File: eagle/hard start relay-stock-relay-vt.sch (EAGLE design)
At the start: 0 parts

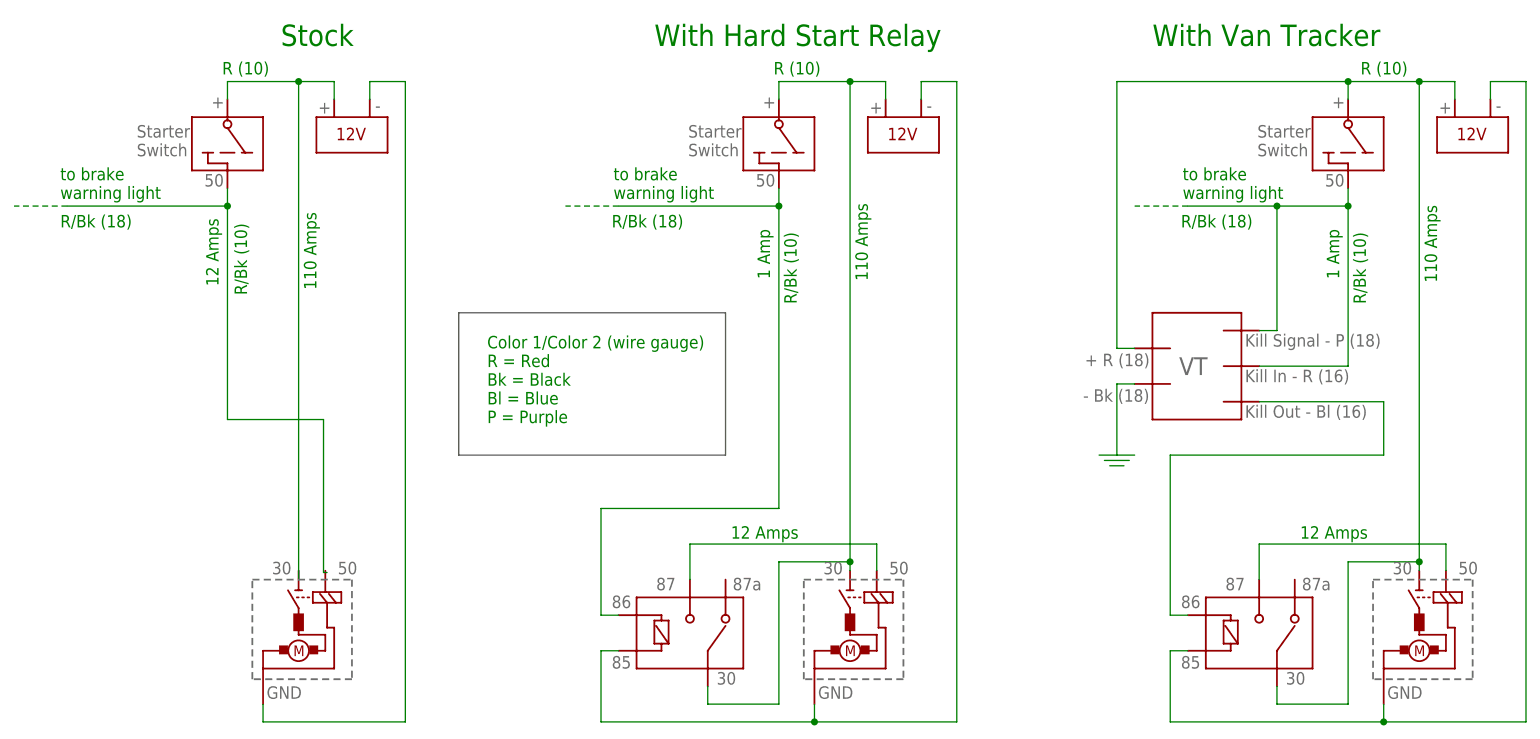
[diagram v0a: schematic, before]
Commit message: 1.kill signal is now also the line that's being interrupted 2.remove starter wire that goes to emergency brake warning light, etc.
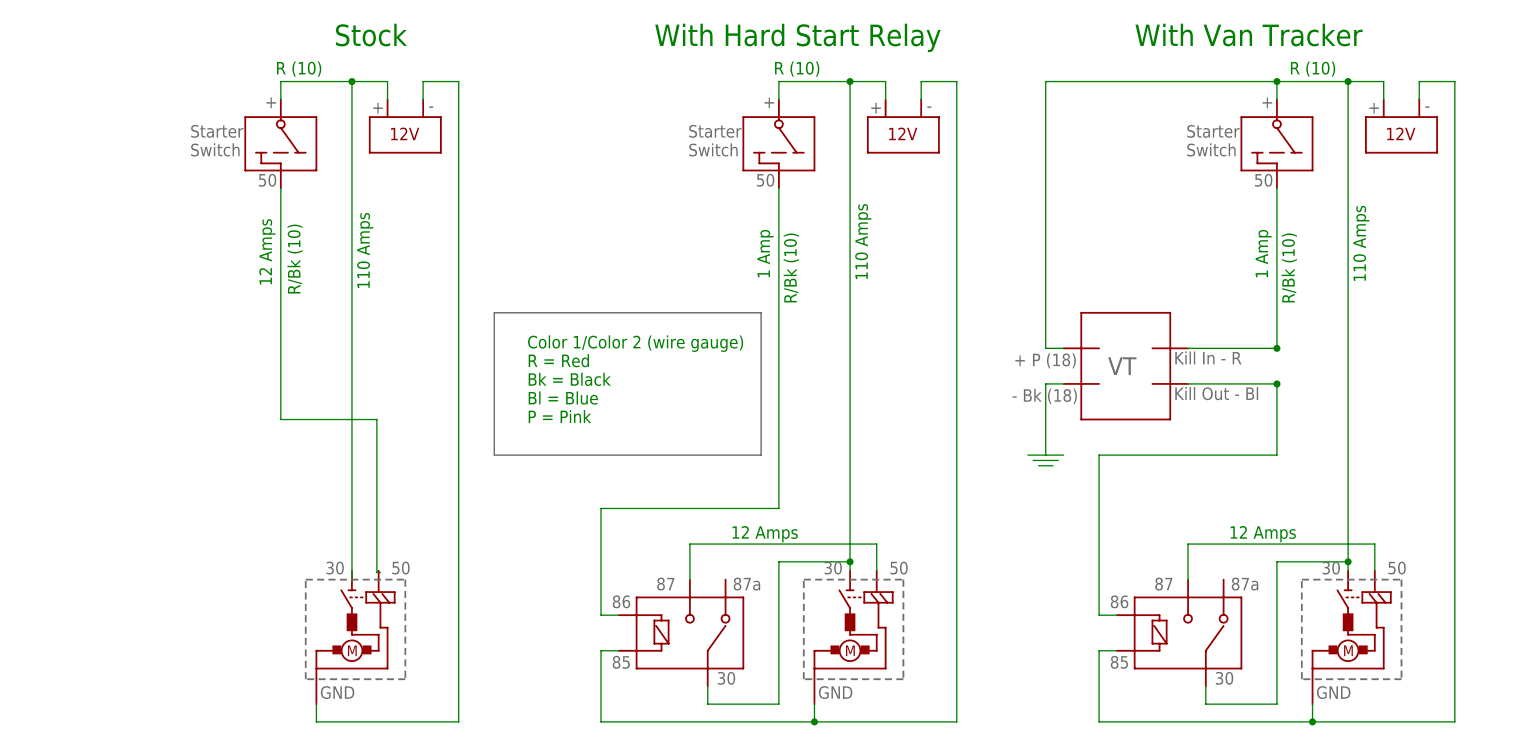
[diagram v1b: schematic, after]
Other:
- note added: "Color 1/Color 2 (wire gauge) R = Red Bk = Black Bl = Blue P = Pink"
- note removed: "Color 1/Color 2 (wire gauge) R = Red Bk = Black Bl = Blue P = Purple"
- note removed: "R/Bk (18)"
- note removed: "to brake warning light"
